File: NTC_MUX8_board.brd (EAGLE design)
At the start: 76.2 x 50.8 mm, 59 parts, among them IC1 NINA-B306-00B, IC2 INA126E, IC3 MCP6001T_SOT23, IC4 MAX8559ETAAA+T, J1 USB4105-GF-A, J2 1761681-7, J3 DM3CS-SF-PEJMS, J4 DNP, Q1 NTR5103NT1G, Q2 NTR5103NT1G, T1N TESTPOINT_TPS-SMD-10SN, T1P TESTPOINT_TPS-SMD-10SN, U1 TMUX1208PWR, U2 TMUX1208PWR, U3 TMUX1208PWR, U4 TMUX1208PWR

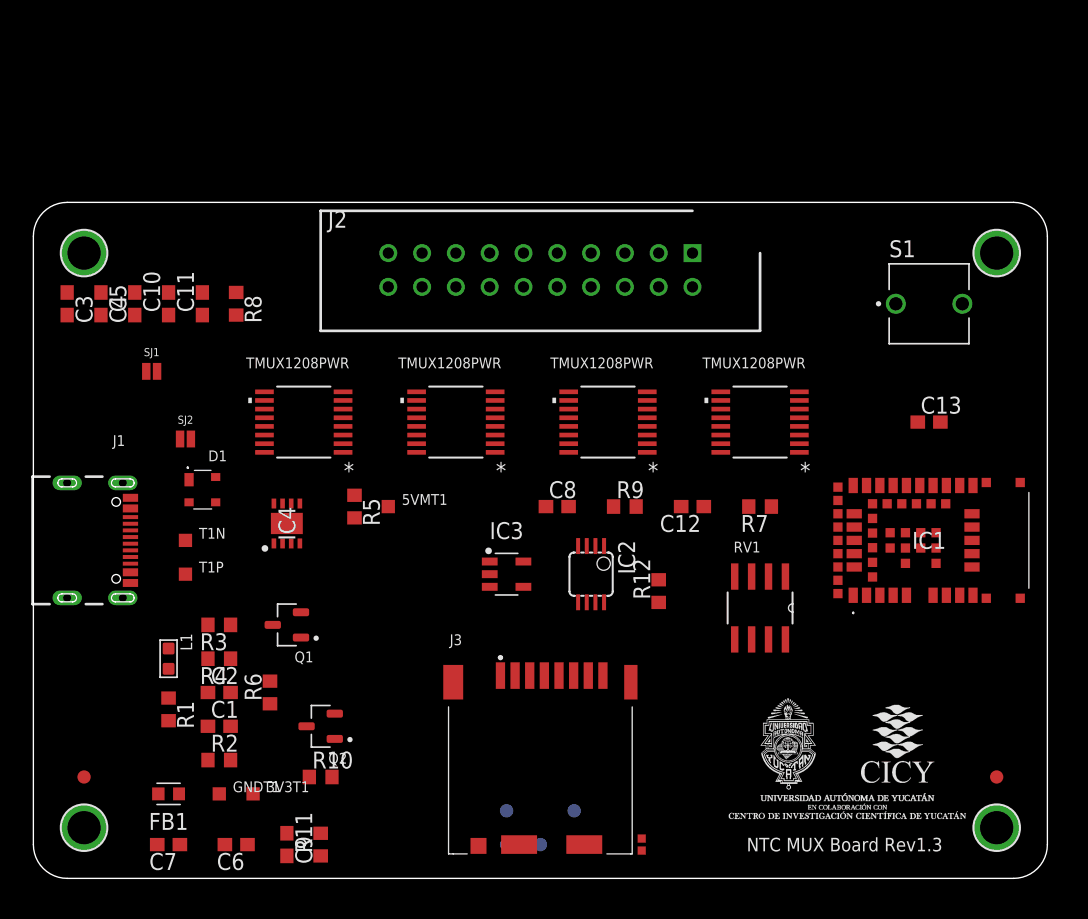
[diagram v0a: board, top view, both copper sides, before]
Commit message: 3d models updated
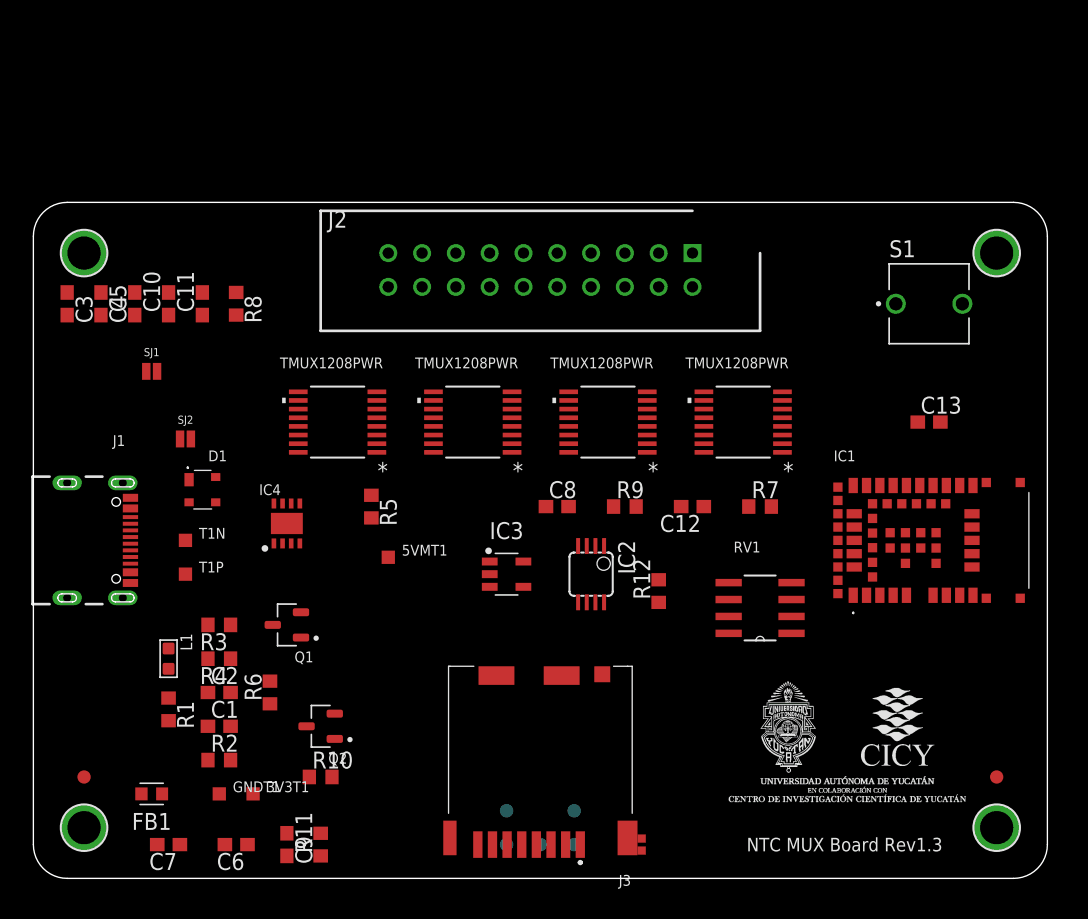
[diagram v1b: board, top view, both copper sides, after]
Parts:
- moved 5VMT1 3.81 mm to (26.7, 24.1)
- moved U2 2.54 mm to (22.9, 34.3)
- moved U1 1.27 mm to (33.0, 34.3)
- moved U$5 1.27 mm to (52.1, 5.08)
- moved FB1 1.27 mm to (8.89, 6.35)
- moved R5 1.27 mm to (25.4, 27.9)
- moved U4 1.27 mm to (53.3, 34.3)
- turned J3 to 0 degrees
- turned R7 to 0 degrees
- turned RV1 to 180 degrees
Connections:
- new net N$10: R4.1
- net RESETN: now also IC1.19
- net SWCLK: now also IC1.11
- net SWDIO: now also IC1.15
- net V_USB: no longer R4.1

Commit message: detalles
faltan los detalles marcados en el esquemático
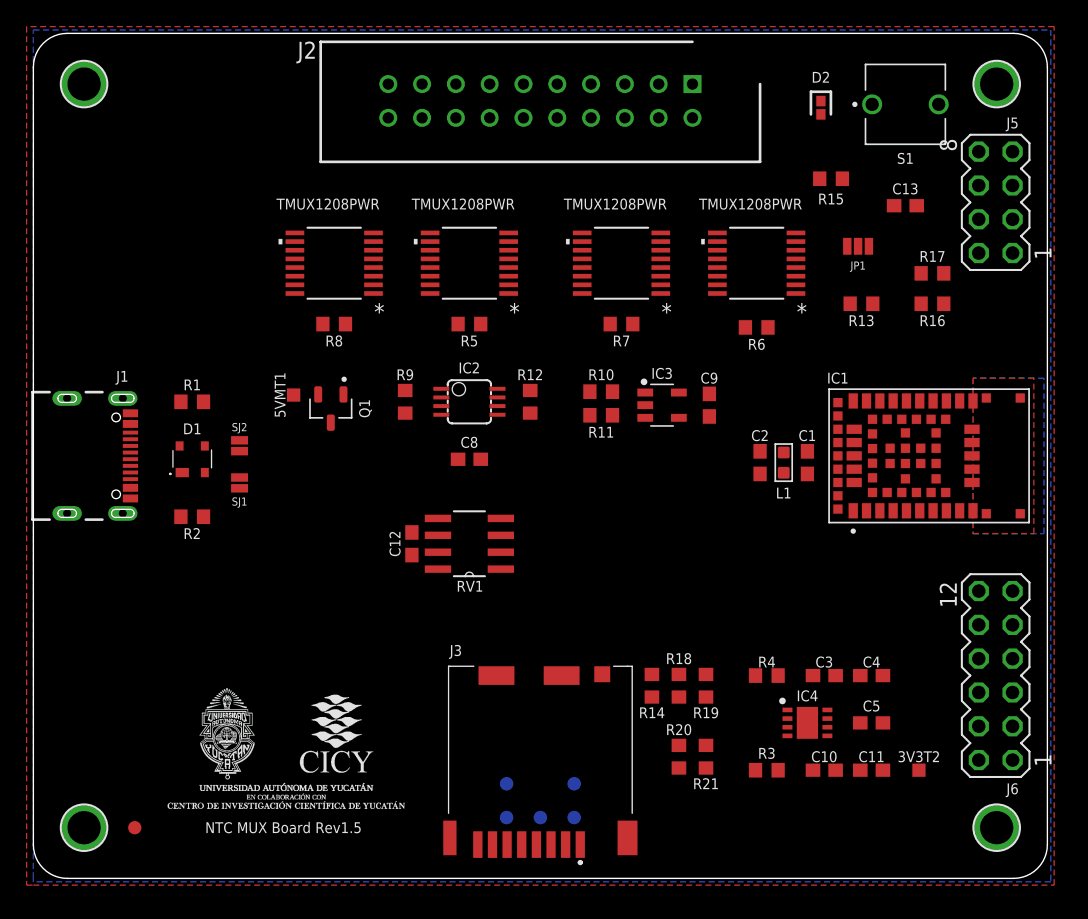
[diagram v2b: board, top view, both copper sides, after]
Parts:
- removed 3V3T1, GNDT1, T1N, T1P: TESTPOINT_TPS-SMD-10SN, 52101-101-REV-A_v16:TESTPOINT_SMD-10SN
- removed C6, C7: 1n, rcl:C0603
- removed FB1: FERRITE_BEAD, Filter:BEADC1608X95N
- removed FID4: FIDUCIAL_1MM, microbuilder:FIDUCIAL_1MM
- removed Q2: NTR5103NT1G, NTR5103NT1G:SOT95P237X111-3N
- added 3V3T2: TESTPOINT_TPS-SMD-10SN, 52101-101-REV-A_v16:TESTPOINT_SMD-10SN
- added D2: SML-P12PTT86R, SML-P12PTT86R:LEDC1006X25N
- added J5: (no value), con-lstb:MA04-2
- added J6: (no value), con-lstb:MA06-2
- added JP1: JUMPER-SMT_3_NO_NO-SILK, SparkFun-Jumpers:SMT-JUMPER_3_NO_NO-SILK
- added R14: DNP, rcl:R0603
- added R15: 1k, rcl:R0603
- added R16, R17: 4k7, rcl:R0603
- added R18, R19, R20, R21: 10k, rcl:R0603
- IC1: value NINA-B306-00B -> NINA-B306-00B-00; device NINA-B306-00B:NINAB30600B -> NINA-B306-00B-00:XCVR_NINA-B306-00B-00
- R13: device Arduino-rcl:0402-1005X55N -> rcl:R0603
- moved C4 64.3 mm to (63.0, 15.2), turned to 0 degrees
- moved C5 63.7 mm to (63.0, 11.7), turned to 0 degrees
- moved C3 63.4 mm to (59.4, 15.2), turned to 180 degrees
- moved C11 61.3 mm to (63.0, 8.13), turned to 180 degrees
- moved C10 60.5 mm to (59.4, 8.13), turned to 0 degrees
- moved L1 48.5 mm to (56.4, 31.2), turned to 90 degrees
- moved C1 48.4 mm to (58.2, 31.2), turned to 90 degrees
- moved C9 45.8 mm to (50.8, 35.6)
- moved R6 45.7 mm to (54.4, 41.4), turned to 180 degrees
- moved C2 44.2 mm to (54.6, 31.2), turned to 90 degrees
- moved R13 43.9 mm to (62.2, 43.2), turned to 0 degrees
- moved R3 42.6 mm to (55.1, 8.13), turned to 0 degrees
- moved U$5 42.2 mm to (9.91, 4.57)
- moved IC4 41.9 mm to (58.2, 11.7), turned to 0 degrees
- moved R4 41.2 mm to (55.1, 15.2)
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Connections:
- removed net +3V3: J4.1, R13.1
- removed net 3V3MOSFET: 3V3T1.TP, C9.1, IC2.7, IC3.5, Q2.2, R10.1
- removed net CS_U: RV1.1
- removed net MOSFET2: Q2.1
- removed net N$10: R4.1
- removed net SCK_U: RV1.2
- removed net SI_U: RV1.3
- removed net SWCLK: IC1.11, J4.3, R13.2
- removed net V_MIC: C7.2, FB1.2
- new net CS_3: IC1.4, J6.4
- new net CS_4: IC1.5, J6.3
- new net DP_CS: IC1.2, RV1.1
- new net EAGP: IC1.EAGP1, IC1.EAGP2, IC1.EAGP3, IC1.EAGP4
- new net GP_PB: JP1.3
- new net I2C_SCL: IC1.18, J5.1, J5.2, R16.2
- new net I2C_SDA: IC1.20, J5.3, J5.4, R17.2
- new net N$13: R21.1
- new net PWR_LED: IC1.33, R15.2
- new net R_PULLUP: IC1.8, R16.1, R17.1
- new net SD_CS: IC1.3, J3.2
- new net SPI_MISO: IC1.34, J3.7, J6.5, J6.6, R18.1
- new net SPI_MOSI: IC1.35, J3.3, J6.7, J6.8, R19.1, RV1.3
- new net SPI_SCK: IC1.1, J3.5, J6.10, J6.9, R20.1, RV1.2
- new net SWDCLK: IC1.11, J4.3, R14.2
- new net V_EN: IC1.49, IC4.3, R4.2
- net 3V3_1: now also IC1.10, IC1.9, J4.1, R13.2, R14.1, R4.1
- net 3V3_2: now also 3V3T2.TP, C9.1, IC2.7, IC3.5, J3.4, J5.7, J5.8, J6.11, J6.12, R10.1, R18.2, R19.2, R20.2, R21.2; no longer Q2.3
- net EN1: now also IC1.24
- net EN2: now also IC1.23
- net EN3: now also IC1.21
- net EN4: now also IC1.22
- net GND: now also D2.1, IC1.12, IC1.14, IC1.26, IC1.30, IC1.53, IC1.6, IC1.EGP1, IC1.EGP10, IC1.EGP11, IC1.EGP12, IC1.EGP2, IC1.EGP3, IC1.EGP4, IC1.EGP5, IC1.EGP6, IC1.EGP7, IC1.EGP8, IC1.EGP9, J3.10, J3.11, J3.12, J3.13, J3.6, J3.9, J5.5, J5.6, J6.1, J6.2; no longer C6.1, C7.1, GNDT1.TP
- net N$3: now also D2.2, R15.1; no longer IC4.3, R4.2
- net RESET: now also JP1.2, R13.1
- net RESETN: now also JP1.1
- net USB+: no longer T1P.TP
- net USB-: no longer T1N.TP
- net USB_N: now also IC1.55
- net USB_P: now also IC1.54
- net VBUS: now also IC1.31, Q1.3
- net V_ANALOG: now also IC1.25
- net V_USB: no longer C6.2, FB1.1, Q1.3
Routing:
- added copper zone on layer 1, net GND
- added copper zone on layer 16, net GND
- added copper zone on layer 1, net OFF
- added copper zone on layer 16, net TFF
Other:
- board size 76.2 x 50.8 mm -> 76.2 x 63.5 mm
- board text added: "NTC MUX Board Rev1.5"
- board text removed: "NTC MUX Board Rev1.3"

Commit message: Pequeños errores y adición de mejoras
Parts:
- removed 3V3T2, 5VMT1: TESTPOINT_TPS-SMD-10SN, 52101-101-REV-A_v16:TESTPOINT_SMD-10SN
- removed Q1: NTR5103NT1G, NTR5103NT1G:SOT95P237X111-3N
- added 3V3T1, TPSV+: TESTPOINT_TPS-SMD-10SN, 52101-101-REV-A_v16:TESTPOINT_SMD-10SN
- added J7: 52808-2071, 52808-2071:528082071
- added SV1: (no value), con-lstb:MA03-1
- added X1: 22-23-2021, con-molex:22-23-2021
- moved D2 26.2 mm to (53.6, 32.3), turned to 0 degrees
- moved R15 20.6 mm to (56.2, 32.3)
- moved R9 20.4 mm to (48.3, 36.0)
- moved IC2 20.0 mm to (52.8, 36.0)
- moved C8 17.1 mm to (49.7, 33.4), turned to 180 degrees
- moved R12 15.9 mm to (52.8, 39.6), turned to 180 degrees
- moved C12 14.9 mm to (28.6, 40.0), turned to 0 degrees
- moved R3 13.8 mm to (64.1, 18.7), turned to 180 degrees
- moved R13 13.1 mm to (65.8, 55.7)
- moved JP1 12.4 mm to (66.6, 59.0), turned to 270 degrees
- moved RV1 11.8 mm to (28.6, 36.2)
- moved R7 10.9 mm to (55.1, 42.4)
- moved U4 10.9 mm to (55.1, 47.0)
- moved C11 9.70 mm to (56.2, 15.0), turned to 0 degrees
- moved R6 9.45 mm to (45.0, 42.4)
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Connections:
- net EN1 renamed ENI1
- net EN2 renamed ENI2
- removed net 5VMOSFET: 5VMT1.TP, C12.1, Q1.2, RV1.5, RV1.8, U1.13, U1.8, U2.13, U2.8, U3.13, U4.13
- removed net EN3: IC1.21, R6.2, U3.2
- removed net EN4: IC1.22, R7.2, U4.2
- removed net MOSFET1: Q1.1
- removed net N$13: R21.1
- new net DAT: J3.1, J3.8, R21.1
- new net ENO1: IC1.22, R6.2, U3.2
- new net ENO2: IC1.21, R7.2, U4.2
- new net VSEL: C12.1, RV1.5, RV1.8, SV1.2, TPSV+.TP, U1.13, U1.8, U2.13, U2.8, U3.13, U4.13
- net 3V3_1: now also 3V3T1.TP
- net 3V3_2: now also SV1.3; no longer 3V3T2.TP
- net AIN0: now also IC1.49
- net AIN1: now also IC1.27
- net AIN2: now also IC1.44
- net AOUT0: now also IC1.39
- net AOUT1: now also IC1.41
- net AOUT2: now also IC1.43
- net C1IN: now also J2.20, J7.20, U2.4; no longer J2.19, U1.11
- net C1OUT: now also J2.9, J7.9, U4.4; no longer J2.10, U3.11
- net C2IN: now also J2.18, J7.18, U2.5; no longer J2.17, U1.10
- net C2OUT: now also J2.7, J7.7, U4.5; no longer J2.8, U3.10
- net C3IN: now also J2.16, J7.16, U2.6; no longer J2.15, U1.9
- net C3OUT: now also J2.5, J7.5, U4.6; no longer J2.6, U3.9
- net C4IN: now also J2.14, J7.14, U2.7; no longer J2.13, U2.4
- net C4OUT: now also J2.3, J7.3, U4.7; no longer J2.4, U4.4
- net C5IN: now also J2.12, J7.12, U2.12; no longer J2.11, U2.5
- net C5OUT: now also J2.1, J7.1, U4.12; no longer J2.2, U4.5
- net CS_3: now also J6.3; no longer J6.4
- net CS_4: now also J6.4; no longer J6.3
- net F1IN: now also J2.19, J7.19; no longer J2.20
- net F1OUT: now also J2.10, J7.10; no longer J2.9
- net F2IN: now also J2.17, J7.17; no longer J2.18
- net F2OUT: now also J2.8, J7.8; no longer J2.7
- net F3IN: now also J2.15, J7.15; no longer J2.16
- net F3OUT: now also J2.6, J7.6; no longer J2.5
- net F4IN: now also J2.13, J7.13; no longer J2.14
- net F4OUT: now also J2.4, J7.4; no longer J2.3
- net F5IN: now also J2.11, J7.11; no longer J2.12
- net F5OUT: now also J2.2, J7.2; no longer J2.1
- net GND: now also X1.1
- net GP_PB: now also IC1.37
- net VBUS: no longer Q1.3
- net V_EN: now also IC1.50; no longer IC1.49
- net V_USB: now also SV1.1, X1.2
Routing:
- net 3V3_2: track 0.00 -> 168.2 mm, vias 0 -> 8
- net GND: track 0.00 -> 142.6 mm, vias 0 -> 24
- net V_USB: track 0.00 -> 134.6 mm, vias 0 -> 5
- net SPI_MOSI: track 0.00 -> 125.0 mm, vias 0 -> 3
- net SPI_SCK: track 0.00 -> 111.6 mm, vias 0 -> 5
- net VSEL: track 0.00 -> 104.3 mm, vias 0 -> 4
- net 3V3_1: track 0.00 -> 101.0 mm, vias 0 -> 3
- net RESETN: track 0.00 -> 80.6 mm, vias 0 -> 2
- net SPI_MISO: track 0.00 -> 70.8 mm, vias 0 -> 1
- net AIN0: track 0.00 -> 58.7 mm, vias 0 -> 5
- net SD_CS: track 0.00 -> 57.6 mm, vias 0 -> 2
- net AIN1: track 0.00 -> 55.1 mm, vias 0 -> 4
- net ENI1: track 0.00 -> 55.1 mm, vias 0 -> 2
- net AIN2: track 0.00 -> 54.6 mm, vias 0 -> 4
- net USB_P: track 0.00 -> 50.5 mm, vias 0 -> 2
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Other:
- board text added: "C"
- board text added: "C'"
- board text added: "F"
- board text added: "F'"

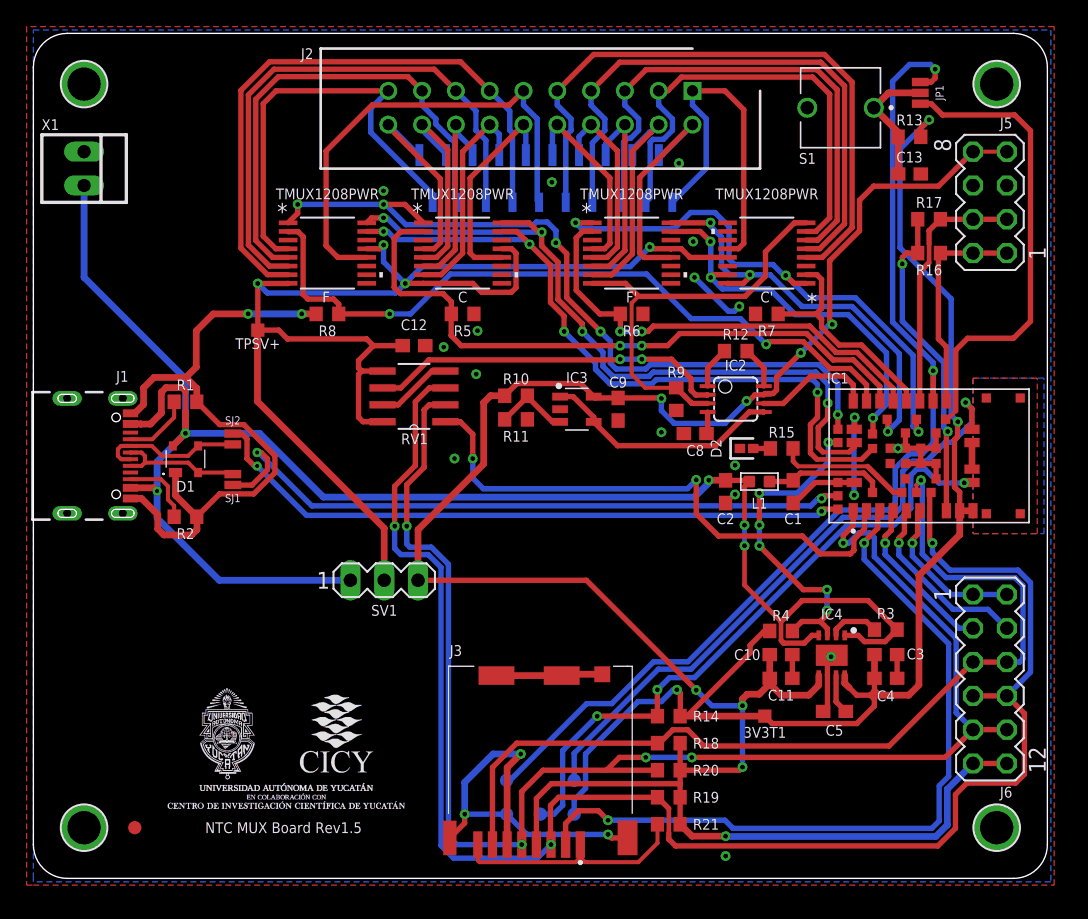
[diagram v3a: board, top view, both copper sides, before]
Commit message: casi listo
añadidas etiquetas y mejora del ruteo de algunas pistas
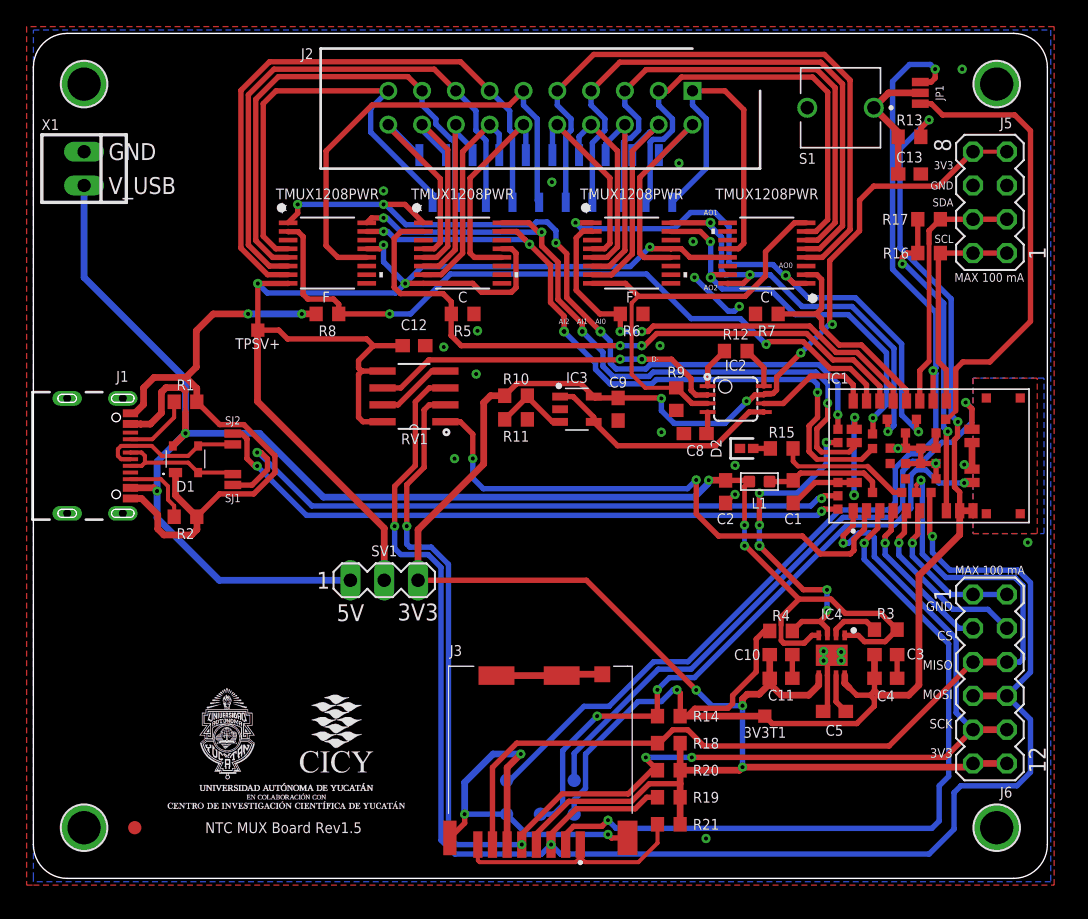
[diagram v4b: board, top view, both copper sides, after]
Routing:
- net 3V3_2: track 168.2 -> 157.8 mm, vias 8 -> 7
- net SPI_MOSI: track 125.0 -> 129.6 mm
- net SPI_SCK: track 111.6 -> 107.7 mm
- net 3V3_1: track 101.0 -> 102.4 mm
- net SD_CS: track 57.6 -> 56.5 mm
- net GP_PB: track 35.5 -> 34.7 mm
- net V_USB: track 134.6 -> 133.8 mm
- net GND: track 142.6 -> 143.4 mm, vias 24 -> 32
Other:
- board text added: "3V3"
- board text added: "3V3 GND SDA SCL"
- board text added: "5V"
- board text added: "AI0"
- board text added: "AI1"
- board text added: "AI2"
- board text added: "AO0"
- board text added: "AO1"
- board text added: "AO2"
- board text added: "C1IN"
- board text added: "C1OUT"
- board text added: "C3IN"
- board text added: "C3OUT"
- board text added: "C5IN"
- board text added: "C5OUT"
- board text added: "D-"
- board text added: "F1IN"
- board text added: "F1OUT"
- board text added: "F3IN"
- board text added: "F3OUT"
- board text added: "F5IN"
- board text added: "F5OUT"
- board text added: "GND"
- board text added: "GND CS MISO MOSI SCK 3V3"
- board text added: "GND V_USB"
- board text added: "MAX 100 mA"
- board text added: "SCL"
- board text added: "SDA"

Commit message: beta finalizada
circuito listo a mi parecer
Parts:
- added C6, C7: 100nF, rcl:C0603
- C10, C3: value 2.2uF -> 100nF
- C11, C4: value 2.2uF -> 10uF
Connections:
- net 3V3_1: now also C6.1, C7.1
- net GND: now also C6.2, C7.2
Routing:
- net 3V3_1: track 102.4 -> 105.4 mm
